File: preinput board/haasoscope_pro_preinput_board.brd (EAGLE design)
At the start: 94.2 x 41.9 mm, 31 parts, among them J4 8pin, K1 G6K-2F-RF-T-TR03_DC5, K2 G6K-2F-RF-T-TR03_DC5, K3 TLP3440_TP,F, K5 G6K-2F-RF-T-TR03_DC5, Q1 S8050, Q2 S8050, Q3 S8050

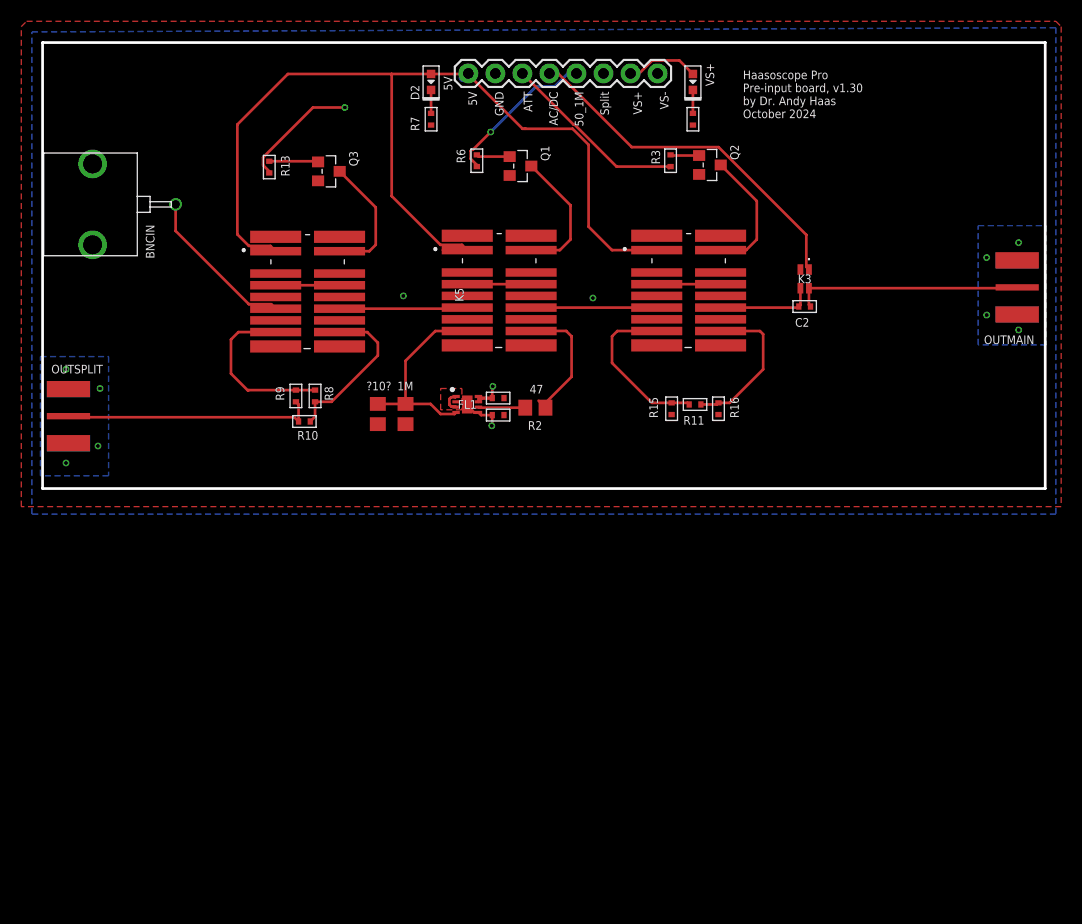
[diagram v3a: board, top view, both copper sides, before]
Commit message: try no thermals, cutouts under relays
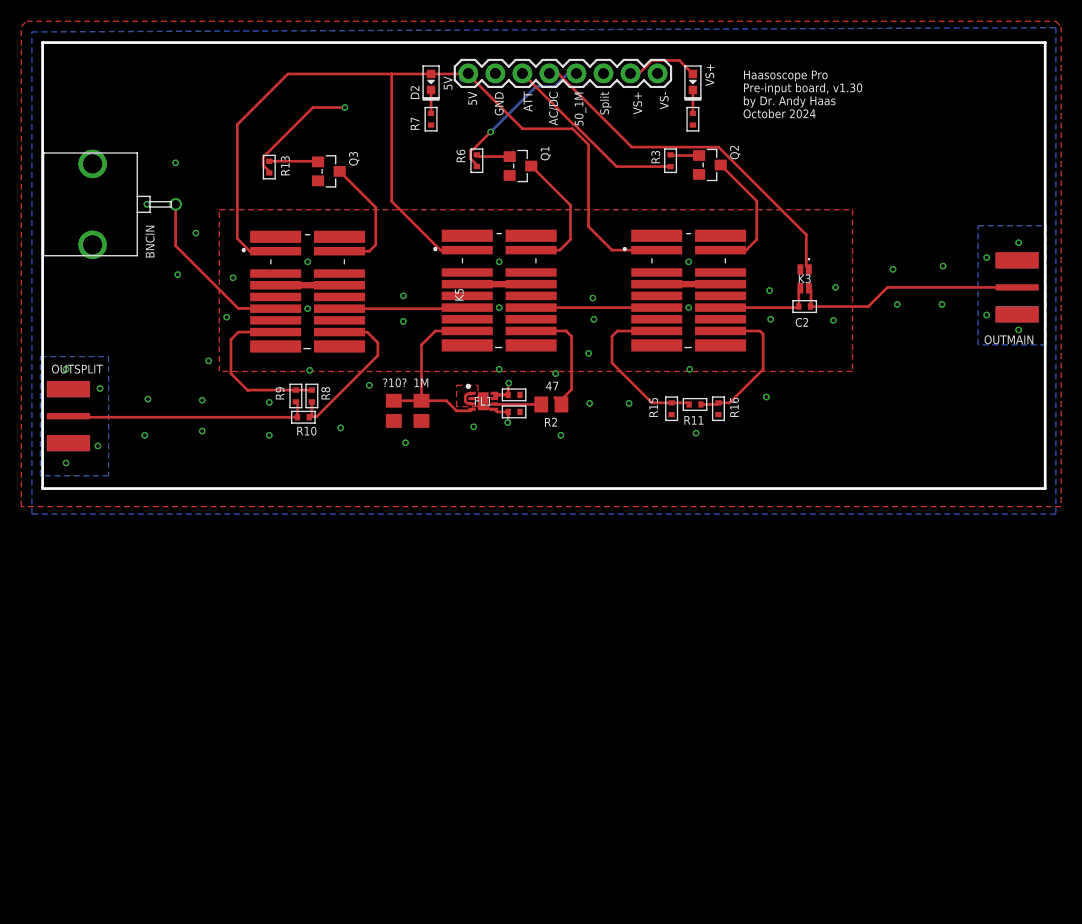
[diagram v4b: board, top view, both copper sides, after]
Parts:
- moved FL1 1.53 mm to (32.2, 16.3)
- moved C1 1.53 mm to (23.8, 15.4)
- moved C12 1.53 mm to (35.1, 15.3)
- moved R1 1.53 mm to (26.4, 15.4)
- moved R2 1.53 mm to (38.6, 16.0)
- moved C11 1.53 mm to (35.1, 16.9)
- moved R10 0.41 mm to (15.3, 14.8)
- moved R8 0.30 mm to (16.1, 16.8)
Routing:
- net 1MPATH50: track 12.6 -> 11.7 mm
- net 1MPATH: track 18.8 -> 17.9 mm
- net INPATH: track 14.9 -> 15.7 mm
- net OUTSPLIT: track 24.8 -> 24.1 mm
- net OUTMAIN: track 21.4 -> 22.0 mm
- net SPLITOUT: track 15.0 -> 15.5 mm
- net 5V: track 91.9 -> 92.4 mm

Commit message: rename photoMOS to 3475R
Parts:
- K3: value TLP3440_TP,F -> TLP3475R_TP,F; device TLP3440_TP_F:TLP3440TPF -> TLP3475R_TP_F:TLP3475RTPF
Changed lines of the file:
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@@
 <attribute name="VALUE" x="33.7" y="33.45" size="0.8128" layer="27" align="center"/>
 </element>
-<element name="K3" library="TLP3440_TP_F" package="TLP3440TPF" value="TLP3440_TP,F" x="62.4" y="27.8" smashed="yes" rot="R180">
+<element name="K3" library="TLP3475R_TP_F" package="TLP3475RTPF" value="TLP3475R_TP,F" x="62.4" y="27.8" smashed="yes" rot="R180">
 <attribute name="DESCRIPTION" value="Solid State Relays - PCB Mount Photorelay Voff=40V Ion=0.12A Ron=14Ohm" x="62.4" y="27.8" size="1.778" layer="27" rot="R180" display="off"/>
 <attribute name="HEIGHT" value="1.4mm" x="62.4" y="27.8" size="1.778" layer="27" rot="R180" display="off"/>
@@
 <attribute name="MANUFACTURER_NAME" value="Toshiba" x="62.4" y="27.8" size="1.778" layer="27" rot="R180" display="off"/>
 <attribute name="MANUFACTURER_PART_NUMBER" value="TLP3475R(TP,F" x="62.4" y="27.8" size="1.778" layer="27" rot="R180" display="off"/>
-<attribute name="MOUSER_PART_NUMBER" value="757-TLP3440TPF" x="62.4" y="27.8" size="1.778" layer="27" rot="R180" display="off"/>
-<attribute name="MOUSER_PRICE-STOCK" value="https://www.mouser.co.uk/ProductDetail/Toshiba/TLP3440TPF?qs=bYcAidFZG4jqnlmzhh150Q%3D%3D" x="62.4" y="27.8" size="1.778" layer="27" rot="R180" display="off"/>
+<attribute name="MOUSER_PART_NUMBER" value="757-TLP3475RTPF" x="62.4" y="27.8" size="1.778" layer="27" rot="R180" display="off"/>
+<attribute name="MOUSER_PRICE-STOCK" value="https://www.mouser.co.uk/ProductDetail/Toshiba/TLP3475RTPF?qs=bYcAidFZG4jqnlmzhh150Q%3D%3D" x="62.4" y="27.8" size="1.778" layer="27" rot="R180" display="off"/>
 <attribute name="NAME" x="62.4" y="27.8" size="0.8128" layer="25" rot="R180" align="center"/>
 <attribute name="VALUE" x="62.4" y="30.7" size="0.8128" layer="27" rot="R180" align="center"/>
